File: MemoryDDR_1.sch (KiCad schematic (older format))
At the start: 26 parts

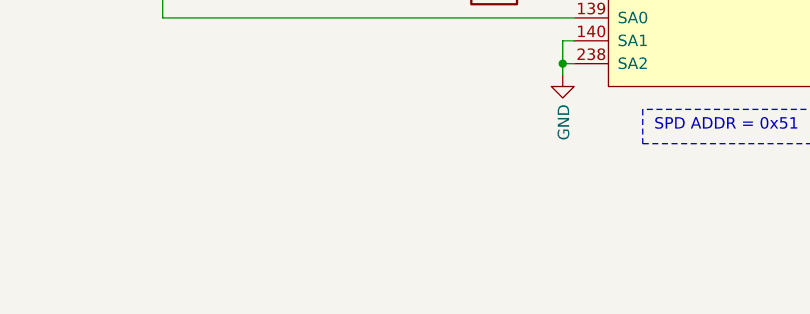
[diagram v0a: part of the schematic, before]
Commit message: RAM - Add description for control signals voltage reference
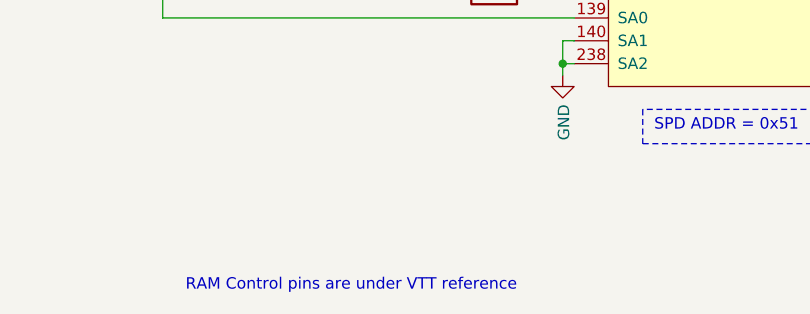
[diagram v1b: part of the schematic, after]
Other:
- note added: "RAM Control pins are under VTT reference"
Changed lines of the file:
@@
 	1    0    0    -1
 $EndComp
+Text Notes 6200 11050 0    50   ~ 0
+RAM Control pins are under VTT reference
 Wire Bus Line
 	7050 3150 7050 3450
